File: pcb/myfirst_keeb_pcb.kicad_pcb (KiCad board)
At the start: 2 copper layers, 28 parts, among them SW1 SW_Push, U1 SRV05-4, U2 ATmega32U4-AU, Y1 16MHz

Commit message: Assign 1u+ key footprints Half arranged layout
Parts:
- removed R4: 10k, Resistor_SMD:R_0805_2012Metric
- removed Y1: 16MHz, Crystal:Crystal_SMD_3225-4Pin_3.2x2.5mm
- added D10: SOD_123, Diode_SMD:D_SOD-123, F.Cu at (272.8, 170.2)
- added D11: SOD_123, Diode_SMD:D_SOD-123, F.Cu at (267.0, 173.5)
- added D12: SOD_123, Diode_SMD:D_SOD-123, F.Cu at (261.3, 176.9)
- added D13: SOD_123, Diode_SMD:D_SOD-123, F.Cu at (267.0, 170.2)
- added D14: SOD_123, Diode_SMD:D_SOD-123, F.Cu at (261.3, 173.5)
- added D15: SOD_123, Diode_SMD:D_SOD-123, F.Cu at (272.8, 166.8)
- added D16: SOD_123, Diode_SMD:D_SOD-123, F.Cu at (255.5, 176.9)
- added D17: SOD_123, Diode_SMD:D_SOD-123, F.Cu at (249.8, 176.9)
- added D18: SOD_123, Diode_SMD:D_SOD-123, F.Cu at (244.0, 176.9)
- added D19: SOD_123, Diode_SMD:D_SOD-123, F.Cu at (255.5, 173.5)
- added D20: SOD_123, Diode_SMD:D_SOD-123, F.Cu at (249.8, 173.5)
- added D21: SOD_123, Diode_SMD:D_SOD-123, F.Cu at (226.8, 176.9)
- added D22: SOD_123, Diode_SMD:D_SOD-123, F.Cu at (267.0, 166.8)
- added D23: SOD_123, Diode_SMD:D_SOD-123, F.Cu at (261.3, 166.8)
- added D24: SOD_123, Diode_SMD:D_SOD-123, F.Cu at (255.5, 166.8)
- added D25: SOD_123, Diode_SMD:D_SOD-123, F.Cu at (249.8, 170.2)
- added D26: SOD_123, Diode_SMD:D_SOD-123, F.Cu at (244.0, 170.2)
- added D27: SOD_123, Diode_SMD:D_SOD-123, F.Cu at (238.3, 176.9)
- added D28: SOD_123, Diode_SMD:D_SOD-123, F.Cu at (226.8, 173.5)
- added D29: SOD_123, Diode_SMD:D_SOD-123, F.Cu at (232.5, 176.9)
- added D30: SOD_123, Diode_SMD:D_SOD-123, F.Cu at (255.5, 170.2)
- added D31: SOD_123, Diode_SMD:D_SOD-123, F.Cu at (238.3, 173.5)
- added D32: SOD_123, Diode_SMD:D_SOD-123, F.Cu at (232.5, 173.5)
- added D33: SOD_123, Diode_SMD:D_SOD-123, F.Cu at (238.3, 170.2)
- added D34: SOD_123, Diode_SMD:D_SOD-123, F.Cu at (244.0, 166.8)
- added D35: SOD_123, Diode_SMD:D_SOD-123, F.Cu at (238.3, 166.8)
- added D36: SOD_123, Diode_SMD:D_SOD-123, F.Cu at (232.5, 170.2)
- added D37: SOD_123, Diode_SMD:D_SOD-123, F.Cu at (249.8, 166.8)
- added D38: SOD_123, Diode_SMD:D_SOD-123, F.Cu at (244.0, 173.5)
- added D39: SOD_123, Diode_SMD:D_SOD-123, F.Cu at (186.5, 170.2)
- added D40: SOD_123, Diode_SMD:D_SOD-123, F.Cu at (215.3, 166.8)
- added D41: SOD_123, Diode_SMD:D_SOD-123, F.Cu at (221.0, 176.9)
- added D42: SOD_123, Diode_SMD:D_SOD-123, F.Cu at (226.8, 170.2)
- added D43: SOD_123, Diode_SMD:D_SOD-123, F.Cu at (221.0, 173.5)
- added D44: SOD_123, Diode_SMD:D_SOD-123, F.Cu at (232.5, 166.8)
- added D45: SOD_123, Diode_SMD:D_SOD-123, F.Cu at (215.3, 176.9)
- added D46: SOD_123, Diode_SMD:D_SOD-123, F.Cu at (209.5, 176.9)
- added D47: SOD_123, Diode_SMD:D_SOD-123, F.Cu at (203.8, 176.9)
- added D48: SOD_123, Diode_SMD:D_SOD-123, F.Cu at (215.3, 173.5)
- added D49: SOD_123, Diode_SMD:D_SOD-123, F.Cu at (209.5, 173.5)
- added D5: SOD_123, Diode_SMD:D_SOD-123, F.Cu at (221.0, 166.8)
- added D50: SOD_123, Diode_SMD:D_SOD-123, F.Cu at (203.8, 173.5)
- added D51: SOD_123, Diode_SMD:D_SOD-123, F.Cu at (221.0, 170.2)
- added D52: SOD_123, Diode_SMD:D_SOD-123, F.Cu at (215.3, 170.2)
- added D53: SOD_123, Diode_SMD:D_SOD-123, F.Cu at (226.8, 166.8)
- added D54: SOD_123, Diode_SMD:D_SOD-123, F.Cu at (192.3, 166.8)
- added D55: SOD_123, Diode_SMD:D_SOD-123, F.Cu at (186.7, 166.4)
- added D56: SOD_123, Diode_SMD:D_SOD-123, F.Cu at (209.5, 170.2)
- added D57: SOD_123, Diode_SMD:D_SOD-123, F.Cu at (203.8, 170.2)
- added D58: SOD_123, Diode_SMD:D_SOD-123, F.Cu at (198.0, 176.9)
- added D59: SOD_123, Diode_SMD:D_SOD-123, F.Cu at (209.5, 166.8)
- added D6: SOD_123, Diode_SMD:D_SOD-123, F.Cu at (261.3, 170.2)
- added D60: SOD_123, Diode_SMD:D_SOD-123, F.Cu at (192.3, 176.9)
- added D61: SOD_123, Diode_SMD:D_SOD-123, F.Cu at (186.5, 176.9)
- added D62: SOD_123, Diode_SMD:D_SOD-123, F.Cu at (198.0, 173.5)
- added D63: SOD_123, Diode_SMD:D_SOD-123, F.Cu at (192.3, 173.5)
- added D64: SOD_123, Diode_SMD:D_SOD-123, F.Cu at (186.5, 173.5)
- added D65: SOD_123, Diode_SMD:D_SOD-123, F.Cu at (198.0, 170.2)
- added D66: SOD_123, Diode_SMD:D_SOD-123, F.Cu at (203.8, 166.8)
- added D67: SOD_123, Diode_SMD:D_SOD-123, F.Cu at (198.0, 166.8)
- added D68: SOD_123, Diode_SMD:D_SOD-123, F.Cu at (192.3, 170.2)
- added D7: SOD_123, Diode_SMD:D_SOD-123, F.Cu at (278.5, 170.2)
- added D8: SOD_123, Diode_SMD:D_SOD-123, F.Cu at (284.3, 166.8)
- added D9: SOD_123, Diode_SMD:D_SOD-123, F.Cu at (278.5, 166.8)
- added MX10: 2, MX_Alps_Hybrid:MX-1U-NoLED, F.Cu at (157.7, -85.4)
- added MX11: W, MX_Alps_Hybrid:MX-1U-NoLED, F.Cu at (167.2, -66.4)
- added MX12: S, MX_Alps_Hybrid:MX-1U-NoLED, F.Cu at (172.0, -47.3)
- added MX13: Z, MX_Alps_Hybrid:MX-1U-NoLED, F.Cu at (395.8, 74.3)
- added MX14: Super, MX_Alps_Hybrid:MX-1.25U-NoLED, F.Cu at (375.6, 94.5)
- added MX15: 3, MX_Alps_Hybrid:MX-1U-NoLED, F.Cu at (176.7, -85.4)
- added MX16: E, MX_Alps_Hybrid:MX-1U-NoLED, F.Cu at (186.2, -66.4)
- added MX17: D, MX_Alps_Hybrid:MX-1U-NoLED, F.Cu at (191.0, -47.3)
- added MX18: X, MX_Alps_Hybrid:MX-1U-NoLED, F.Cu at (395.8, 54.1)
- added MX19: LAlt, MX_Alps_Hybrid:MX-1.25U-NoLED, F.Cu at (375.6, 74.3)
- added MX20: 4, MX_Alps_Hybrid:MX-1U-NoLED, F.Cu at (195.8, -85.4)
- added MX21: R, MX_Alps_Hybrid:MX-1U-NoLED, F.Cu at (205.3, -66.4)
- added MX22: F, MX_Alps_Hybrid:MX-1U-NoLED, F.Cu at (210.1, -47.3)
- added MX23: C, MX_Alps_Hybrid:MX-1U-NoLED, F.Cu at (294.8, 94.5)
- added MX24: 5, MX_Alps_Hybrid:MX-1U-NoLED, F.Cu at (214.8, -85.4)
- added MX25: T, MX_Alps_Hybrid:MX-1U-NoLED, F.Cu at (224.3, -66.4)
- added MX26: G, MX_Alps_Hybrid:MX-1U-NoLED, F.Cu at (229.1, -47.3)
- added MX27: V, MX_Alps_Hybrid:MX-1U-NoLED, F.Cu at (315.0, 94.5)
- added MX28: 6, MX_Alps_Hybrid:MX-1U-NoLED, F.Cu at (233.9, -85.4)
- added MX29: Y, MX_Alps_Hybrid:MX-1U-NoLED, F.Cu at (243.4, -66.4)
- added MX30: H, MX_Alps_Hybrid:MX-1U-NoLED, F.Cu at (248.2, -47.3)
- added MX31: B, MX_Alps_Hybrid:MX-1U-NoLED, F.Cu at (294.8, 134.9)
- added MX32: Space, MX_Alps_Hybrid:MX-6.25U-NoLED, F.Cu at (315.0, 114.7)
- added MX33: 7, MX_Alps_Hybrid:MX-1U-NoLED, F.Cu at (252.9, -85.4)
- added MX34: U, MX_Alps_Hybrid:MX-1U-NoLED, F.Cu at (262.4, -66.4)
- added MX35: J, MX_Alps_Hybrid:MX-1U-NoLED, F.Cu at (267.2, -47.3)
- added MX36: N, MX_Alps_Hybrid:MX-1U-NoLED, F.Cu at (294.8, 155.1)
- added MX37: 8, MX_Alps_Hybrid:MX-1U-NoLED, F.Cu at (272.0, -85.4)
- added MX38: I, MX_Alps_Hybrid:MX-1U-NoLED, F.Cu at (281.4, -66.4)
- added MX39: K, MX_Alps_Hybrid:MX-1U-NoLED, F.Cu at (286.3, -47.3)
- added MX40: M, MX_Alps_Hybrid:MX-1U-NoLED, F.Cu at (254.4, 134.9)
- added MX41: 9, MX_Alps_Hybrid:MX-1U-NoLED, F.Cu at (291.0, -85.4)
- added MX42: O, MX_Alps_Hybrid:MX-1U-NoLED, F.Cu at (300.5, -66.4)
- added MX43: L, MX_Alps_Hybrid:MX-1U-NoLED, F.Cu at (305.3, -47.3)
- added MX44: ,, MX_Alps_Hybrid:MX-1U-NoLED, F.Cu at (274.6, 94.5)
- added MX45: RAlt, MX_Alps_Hybrid:MX-1.25U-NoLED, F.Cu at (254.4, 114.7)
- added MX46: 0, MX_Alps_Hybrid:MX-1U-NoLED, F.Cu at (310.1, -85.4)
- added MX47: P, MX_Alps_Hybrid:MX-1U-NoLED, F.Cu at (319.6, -66.4)
- added MX48: ;, MX_Alps_Hybrid:MX-1U-NoLED, F.Cu at (324.4, -47.3)
- added MX49: ., MX_Alps_Hybrid:MX-1U-NoLED, F.Cu at (274.6, 74.3)
- added MX5: Ctrl, MX_Alps_Hybrid:MX-1.25U-NoLED, F.Cu at (122.0, -9.27)
- added MX50: Fn, MX_Alps_Hybrid:MX-1.25U-NoLED, F.Cu at (254.4, 94.5)
- added MX51: _, MX_Alps_Hybrid:MX-1U-NoLED, F.Cu at (329.1, -85.4)
- added MX52: {, MX_Alps_Hybrid:MX-1U-NoLED, F.Cu at (338.6, -66.4)
- added MX53: ", MX_Alps_Hybrid:MX-1U-NoLED, F.Cu at (343.4, -47.3)
- added MX54: /, MX_Alps_Hybrid:MX-1U-NoLED, F.Cu at (274.6, 54.1)
- added MX55: +, MX_Alps_Hybrid:MX-1U-NoLED, F.Cu at (348.2, -85.4)
- added MX56: }, MX_Alps_Hybrid:MX-1U-NoLED, F.Cu at (357.7, -66.4)
- added MX57: LShift, MX_Alps_Hybrid:MX-2.25U-NoLED, F.Cu at (131.5, -28.3)
- added MX58: Left, MX_Alps_Hybrid:MX-1U-NoLED, F.Cu at (193.8, 134.9)
- added MX59: Backspace, MX_Alps_Hybrid:MX-2U-NoLED, F.Cu at (376.7, -85.4)
- added MX6: 1, MX_Alps_Hybrid:MX-1U-NoLED, F.Cu at (138.6, -85.4)
- added MX60: |, MX_Alps_Hybrid:MX-1.5U-NoLED, F.Cu at (381.5, -66.4)
- added MX61: Enter, MX_Alps_Hybrid:MX-2.25U-NoLED, F.Cu at (374.4, -47.3)
- added MX62: Up, MX_Alps_Hybrid:MX-1U-NoLED, F.Cu at (193.8, 114.7)
- added MX63: Down, MX_Alps_Hybrid:MX-1U-NoLED, F.Cu at (234.2, 54.1)
- added MX64: Del, MX_Alps_Hybrid:MX-1U-NoLED, F.Cu at (214.0, 74.3)
- added MX65: PageUp, MX_Alps_Hybrid:MX-1U-NoLED, F.Cu at (193.8, 94.5)
- added MX66: PageDown, MX_Alps_Hybrid:MX-1U-NoLED, F.Cu at (214.0, 54.1)
- added MX67: Right, MX_Alps_Hybrid:MX-1U-NoLED, F.Cu at (193.8, 74.3)
- added MX7: Q, MX_Alps_Hybrid:MX-1U-NoLED, F.Cu at (148.1, -66.4)
- added MX8: A, MX_Alps_Hybrid:MX-1U-NoLED, F.Cu at (152.9, -47.3)
- added MX9: Fn, MX_Alps_Hybrid:MX-1.25U-NoLED, F.Cu at (395.8, 94.5)
- added SW2: SW_Push, Button_Switch_SMD:SW_SPST_B3S-1000, F.Cu at (445.5, 48.2)
- added SW3: Rotary_Encoder_Switch, Rotary_Encoder:RotaryEncoder_Alps_EC11E-Switch_Vertical_H20mm, F.Cu at (407.9, 49.1)
- added U3: STM32F303CCTx, Package_QFP:LQFP-48_7x7mm_P0.5mm, F.Cu at (434.3, 49.6)
- C1: value 10uF -> 100nF
- C2, C6: value 0.1uF -> 100nF
- C3, C4: value 22pF -> 100nF
- C5: value 0.1uF -> C_Small
- C7: value 1uF -> 100nF
- C8: value 0.1uF -> 4.7uF
- MX1: value MX-NoLED -> ESC
- MX2: value MX-NoLED -> Tab; footprint MX_Alps_Hybrid:MX-1U-NoLED -> MX_Alps_Hybrid:MX-1.5U-NoLED
- MX3: value MX-NoLED -> CapsLk; footprint MX_Alps_Hybrid:MX-1U-NoLED -> MX_Alps_Hybrid:MX-1.75U-NoLED
- MX4: value MX-NoLED -> RShift; footprint MX_Alps_Hybrid:MX-1U-NoLED -> MX_Alps_Hybrid:MX-1.75U-NoLED
- SW1: footprint random-keyboard-parts:SKQG-1155865 -> Button_Switch_SMD:SW_SPST_B3S-1000
- U2: value ATmega32U4-AU -> MCP1700-3302E_SOT23; footprint Package_QFP:TQFP-44_10x10mm_P0.8mm -> Package_TO_SOT_SMD:SOT-23
- moved MX4 301.7 mm to (379.1, -28.2)
- moved MX1 209.1 mm to (119.6, -85.4)
- moved MX2 170.8 mm to (124.3, -66.4)
- moved MX3 149.9 mm to (126.7, -47.3)
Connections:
- net Net-(D1-Pad1) renamed COL3
- C1 pad 1: +5V -> +3V3
- C2 pad 1: +5V -> +3V3
- C3 pad 1: Net-(C3-Pad1) -> SHIELD
- C3 pad 2: SHIELD -> VCC
- C4 pad 1: Net-(C4-Pad1) -> SHIELD
- C4 pad 2: SHIELD -> Net-(C4-Pad2)
- C6 pad 1: +5V -> +3V3
- C7 pad 1: Net-(C7-Pad1) -> +3V3
- C8 pad 1: +5V -> +3V3
- D2 pad 1: Net-(D2-Pad1) -> ROW1
- D4 pad 1: Net-(D2-Pad1) -> ROW3
- F1 pad 2: +5V -> Net-(C4-Pad2)
- MX3 pad 1: COL1 -> COL0
- MX4 pad 1: COL1 -> COL0
- R1 pad 1: Net-(R1-Pad1) -> D+
- R1 pad 2: D+ -> Net-(R1-Pad2)
- R2 pad 1: Net-(R2-Pad1) -> D-
- R2 pad 2: D- -> Net-(R2-Pad2)
- R3 pad 1: +5V -> SHIELD
- SW1 pad 1: SHIELD -> Net-(R3-Pad2)
- SW1 pad 2: Net-(R3-Pad2) -> +3V3
- U2 pad 1: Net-(U2-Pad1) -> SHIELD
- U2 pad 2: +5V -> +3V3
- U2 pad 3: Net-(R2-Pad1) -> Net-(C4-Pad2)
- USB1 pad 5: D- -> Net-(R2-Pad2)
- USB1 pad 6: D+ -> Net-(R1-Pad2)
- USB1 pad 7: D- -> Net-(R2-Pad2)
- USB1 pad 8: D+ -> Net-(R1-Pad2)

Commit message: key layout complete. Diode todo
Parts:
- removed D9: SOD_123, Diode_SMD:D_SOD-123
- removed MX9: Fn, MX_Alps_Hybrid:MX-1.25U-NoLED
- D1, D2, D3: moved to B.Cu
- moved MX13 254.9 mm to (162.4, -28.3)
- moved MX65 254.7 mm to (405.3, -47.3)
- moved MX14 252.1 mm to (145.7, -9.24)
- moved MX62 239.8 mm to (386.3, -28.2)
- moved MX64 237.5 mm to (405.3, -66.4)
- moved MX18 229.6 mm to (181.4, -28.3)
- moved MX67 227.4 mm to (405.3, -9.17)
- moved MX58 225.4 mm to (367.2, -9.13)
- moved D1 223.1 mm to (127.2, -85.8), turned to 90 degrees
- moved MX19 222.3 mm to (169.6, -9.25)
- moved MX66 208.3 mm to (405.3, -28.2)
- moved D2 204.6 mm to (134.5, -66.7), turned to 90 degrees
- moved MX36 187.1 mm to (257.7, -28.3)
- moved D3 185.1 mm to (138.5, -47.2), turned to 90 degrees
- moved MX31 172.5 mm to (238.6, -28.3)
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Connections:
- D1 pad 1: COL3 -> ROW0
- D10 pad 1: COL3 -> ROW0
- D15 pad 1: COL3 -> ROW0
- D20 pad 1: COL3 -> ROW0
- D24 pad 1: COL3 -> ROW0
- D28 pad 1: COL3 -> ROW0
- D33 pad 1: COL3 -> ROW0
- D37 pad 1: COL3 -> ROW0
- D41 pad 1: COL3 -> ROW0
- D46 pad 1: COL3 -> ROW0
- D51 pad 1: COL3 -> ROW0
- D55 pad 1: COL3 -> ROW0
- D59 pad 1: COL3 -> ROW0
- D6 pad 1: COL3 -> ROW0
- D64 pad 1: COL3 -> ROW0
- D64 pad 2: COL3 -> ROW0
- MX14 pad 1: COL2 -> COL1
- MX19 pad 1: COL3 -> COL2
- SW3 pad S2: COL3 -> ROW0
- U3 pad 10: COL3 -> ROW0

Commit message: diode layout complete added case graphics on pcb
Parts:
- D10, D11, D12, D13, D14, D15, D16, D17, D18, D19, D20, D21, D22, D23, D24, D25, D26, D27, D28, D29, D30, D31, D32, D33, D34, D35, D36, D37, D38, D39, D4, D40, D41, D42, D43, D44, D45, D46, D47, D48, D49, D5, D50, D51, D52, D53, D54, D55, D56, D57, D58, D59, D6, D60, D61, D62, D63, D64, D65, D66, D67, D68, D7, D8, SW2, U3, USB1: moved to B.Cu
- moved U3 238.2 mm to (207.4, 122.0)
- moved SW2 235.3 mm to (222.6, 123.6)
- moved D6 214.9 mm to (87.0, 44.6), turned to 90 degrees
- moved D7 211.0 mm to (96.2, 63.9), turned to 90 degrees
- moved D10 208.9 mm to (105.7, 44.7), turned to 90 degrees
- moved D4 204.6 mm to (309.6, 102.0), turned to 90 degrees
- moved D8 201.3 mm to (101.4, 82.7), turned to 90 degrees
- moved D64 194.4 mm to (338.0, 51.7), turned to 90 degrees
- moved D15 191.8 mm to (124.9, 44.6), turned to 90 degrees
- moved D65 188.5 mm to (353.8, 64.1), turned to 90 degrees
- moved D11 187.0 mm to (115.5, 63.9), turned to 90 degrees
- moved D60 178.1 mm to (330.3, 64.4), turned to 90 degrees
- moved D14 175.2 mm to (94.2, 120.8), turned to 90 degrees
- moved D66 171.7 mm to (353.8, 83.4), turned to 90 degrees
- moved D13 170.5 mm to (110.8, 101.8), turned to 90 degrees
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
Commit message: pcb wip
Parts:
- C1, C2, C3, C4, C5, C6, C7, C8, R1, R2, R3, RC2, SW1, U1, U2: moved to B.Cu
- moved R2 233.5 mm to (109.9, 37.0)
- moved F1 200.6 mm to (122.6, 36.9)
- moved RC1 199.7 mm to (95.1, 37.1)
- moved C4 198.7 mm to (117.7, 36.9)
- moved U2 196.2 mm to (113.8, 37.4)
- moved SW1 195.2 mm to (222.6, 114.8)
- moved R1 188.5 mm to (105.7, 38.8)
- moved C7 183.8 mm to (155.3, 111.8)
- moved U1 180.1 mm to (193.4, 114.0)
- moved C5 177.0 mm to (197.8, 126.6), turned to 180 degrees
- moved C3 175.6 mm to (193.0, 126.7)
- moved R3 169.3 mm to (214.0, 127.1)
- moved RC2 149.1 mm to (146.4, 112.6)
- moved C2 147.4 mm to (141.4, 116.1)
- moved C6 147.2 mm to (146.4, 116.0)
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
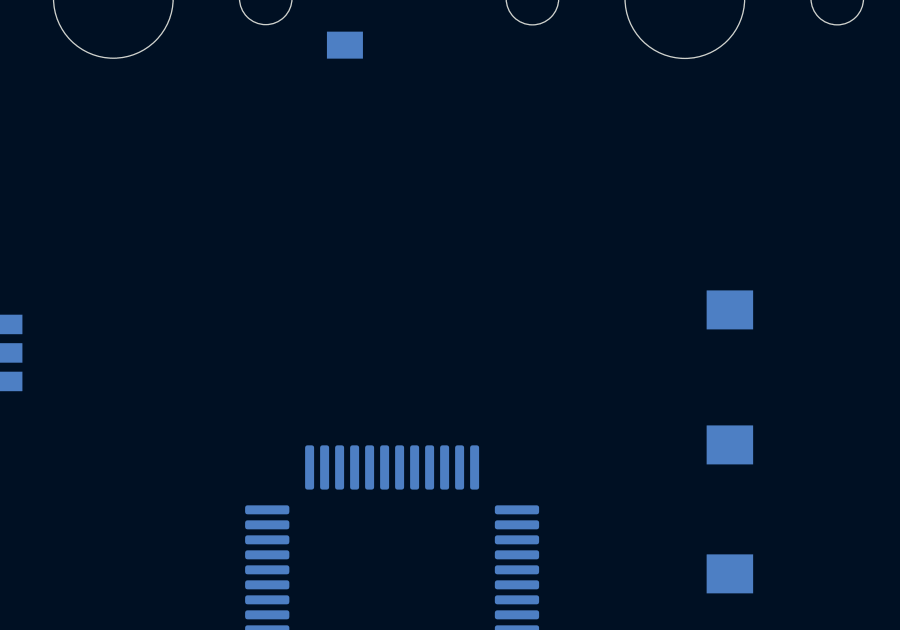
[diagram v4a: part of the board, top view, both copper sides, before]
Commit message: change stm32 chip to STM32F410CBT6
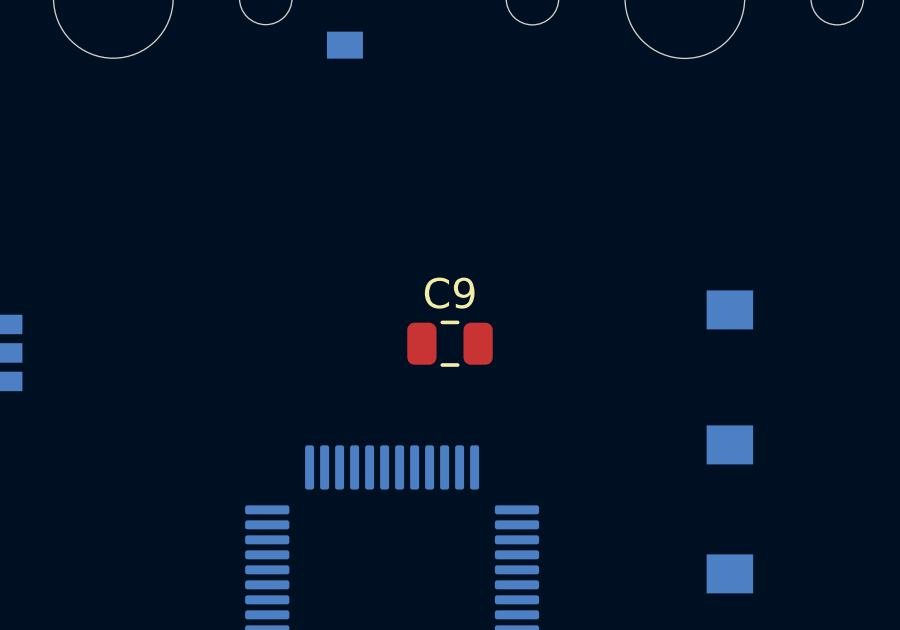
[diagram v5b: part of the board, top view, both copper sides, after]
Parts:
- added C9: 100nF, Capacitor_SMD:C_0805_2012Metric, F.Cu at (209.3, 113.7)
- C5: value C_Small -> 100uF
- U3: value STM32F303CCTx -> STM32F410CBTx
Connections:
- MX4 pad 1: COL0 -> COL12
- MX57 pad 1: COL12 -> COL0
- U3 pad 21: EXTRA_PIN_PB10 -> EXTRA_PIN_PB9
- U3 pad 22: EXTRA_PIN_PB11 -> Net-(C9-Pad1)
- U3 pad 25: EXTRA_PIN_PB12 -> EXTRA_PIN_PB10
- U3 pad 26: EXTRA_PIN_PB13 -> EXTRA_PIN_PB11
- U3 pad 27: EXTRA_PIN_PB14 -> EXTRA_PIN_PB12
- U3 pad 28: EXTRA_PIN_PB15 -> EXTRA_PIN_PB13
- U3 pad 46: EXTRA_PIN_PB9 -> SHIELD
- U3 pad 47: SHIELD -> +3V3

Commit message: complete routing
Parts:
- C9, F1: moved to B.Cu
- RC2: moved to F.Cu
- moved C3 136.4 mm to (93.4, 33.6)
- moved C1 117.6 mm to (72.4, 33.3)
- moved C2 112.0 mm to (48.9, 53.0), turned to 270 degrees
- moved C8 111.1 mm to (48.4, 84.7), turned to 270 degrees
- moved U1 104.4 mm to (123.4, 36.6)
- moved RC2 91.5 mm to (105.1, 31.0), turned to 270 degrees
- moved C6 45.0 mm to (104.0, 131.3)
- moved C4 29.0 mm to (89.2, 31.9), turned to 270 degrees
- moved F1 28.0 mm to (94.6, 36.0), turned to 180 degrees
- moved U2 25.8 mm to (88.1, 36.1)
- moved SW1 20.9 mm to (211.7, 132.6), turned to 270 degrees
- moved C7 19.5 mm to (160.0, 130.7)
- moved R1 12.0 mm to (117.2, 35.3), turned to 180 degrees
- moved C5 9.71 mm to (202.3, 135.2), turned to 90 degrees
- moved SW2 9.16 mm to (220.4, 132.5), turned to 90 degrees
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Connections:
- net SHIELD renamed GND
- D12 pad 1: COL3 -> ROW2
- D14 pad 1: ROW3 -> ROW4
- D17 pad 1: COL3 -> ROW2
- D19 pad 1: ROW3 -> ROW4
- D22 pad 1: COL3 -> ROW2
- D26 pad 1: COL3 -> ROW2
- D3 pad 1: COL3 -> ROW2
- D30 pad 1: COL3 -> ROW2
- D32 pad 1: ROW3 -> ROW4
- D35 pad 1: COL3 -> ROW2
- D39 pad 1: COL3 -> ROW2
- D43 pad 1: COL3 -> ROW2
- D45 pad 1: ROW3 -> ROW4
- D48 pad 1: COL3 -> ROW2
- D5 pad 1: ROW3 -> ROW4
- D50 pad 1: ROW3 -> ROW4
- D53 pad 1: COL3 -> ROW2
- D58 pad 1: ROW3 -> ROW4
- D61 pad 1: COL3 -> ROW2
- D63 pad 1: ROW3 -> ROW4
- D64 pad 2: ROW0 -> Net-(D64-Pad2)
- D66 pad 1: COL3 -> ROW2
- D68 pad 1: ROW3 -> ROW4
- D8 pad 1: COL3 -> ROW2
- MX67 pad 1: COL14 -> (no net)
- MX67 pad 2: Net-(D68-Pad2) -> (no net)
- SW3 pad S2: ROW0 -> Net-(D64-Pad2)
- U3 pad 12: COL3 -> ROW2
- U3 pad 13: ROW3 -> COL0
- U3 pad 14: Audio1 -> COL1
- U3 pad 15: Audio2 -> COL2
- U3 pad 16: COL0 -> COL3
- U3 pad 17: COL1 -> COL4
- U3 pad 2: COL12 -> EXTRA_PIN_PC13
- U3 pad 21: EXTRA_PIN_PB9 -> COL8
- U3 pad 25: EXTRA_PIN_PB10 -> ROW3
- U3 pad 26: EXTRA_PIN_PB11 -> COL14
- U3 pad 27: EXTRA_PIN_PB12 -> COL13
- U3 pad 28: EXTRA_PIN_PB13 -> COL12
- U3 pad 29: COL2 -> COL11
- U3 pad 3: COL13 -> EXTRA_PIN_PC14
- U3 pad 30: COL3 -> COL10
- U3 pad 31: COL4 -> COL9
- U3 pad 38: EXTRA_PIN_PA15 -> ENCODER_A
- U3 pad 39: COL8 -> ENCODER_B
- U3 pad 4: COL14 -> EXTRA_PIN_PC15
- U3 pad 40: COL9 -> ROW4
- U3 pad 5: COL10 -> EXTRA_PIN_PH0
- U3 pad 6: COL11 -> EXTRA_PIN_PH1
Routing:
- net GND: track 0.00 -> 694.6 mm, vias 0 -> 1
- net ROW0: track 0.00 -> 603.5 mm, vias 0 -> 4
- net D+: track 0.00 -> 505.0 mm
- net D-: track 0.00 -> 496.9 mm
- net ROW1: track 0.00 -> 406.1 mm, vias 0 -> 2
- net ROW2: track 0.00 -> 404.3 mm, vias 0 -> 2
- net +3V3: track 0.00 -> 394.0 mm, vias 0 -> 4
- net ROW3: track 0.00 -> 335.1 mm
- net ROW4: track 0.00 -> 313.8 mm, vias 0 -> 3
- net ENCODER_B: track 0.00 -> 291.4 mm, vias 0 -> 1
- net COL0: track 0.00 -> 233.8 mm
- net ENCODER_A: track 0.00 -> 214.4 mm, vias 0 -> 1
- net COL14: track 0.00 -> 211.2 mm
- net COL1: track 0.00 -> 206.3 mm, vias 0 -> 1
- net COL13: track 0.00 -> 203.6 mm
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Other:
- net class Power added: clearance 0.2, trace_width 0.375, via_dia 0.8, via_drill 0.4

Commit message: fix track errors
- hole too close error irrelevant because that is from the mx switch library and its meant to be
- usb pads should be close together, its from the part's library
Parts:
- moved C9 0.77 mm to (210.8, 114.6)
- moved U1 0.68 mm to (123.4, 35.9)
- moved R2 0.35 mm to (118.1, 33.2)
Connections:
- MX67 pad 1: (no net) -> COL14
- MX67 pad 2: (no net) -> Net-(D68-Pad2)
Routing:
- net ENCODER_B: track 291.4 -> 277.0 mm
- net GND: track 694.6 -> 708.4 mm, vias 1 -> 3
- net Net-(C5-Pad1): track 63.8 -> 55.8 mm
- net +3V3: track 394.0 -> 395.9 mm
- net D-: track 496.9 -> 495.7 mm
- net Net-(C9-Pad1): track 2.72 -> 3.54 mm
- net D+: track 505.0 -> 505.8 mm
- net Net-(R2-Pad2): track 19.1 -> 18.6 mm
- added copper zone on B.Cu, net GND
- added copper zone on F.Cu, net GND

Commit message: add cringe deco text
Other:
- board text added: "Zap!"
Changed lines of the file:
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@@
   (general
     (thickness 1.6)
-    (drawings 1998)
+    (drawings 2000)
     (tracks 1037)
     (zones 0)
@@
     )
   )
+  (gr_text Zap! (at 65.6 127.6) (layer F.SilkS)
+    (effects (font (size 8 8) (thickness 1)))
+  )
+  (gr_text Zap! (at 65.6 127.6) (layer B.SilkS)
+    (effects (font (size 8 8) (thickness 1) italic) (justify mirror))
+  )
   (gr_line (start 255.12424 32.13196) (end 255.44824 32.07896) (layer Dwgs.User) (width 0.2))
